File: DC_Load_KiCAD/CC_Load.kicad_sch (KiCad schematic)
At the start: 64 parts, among them J1 VoltSense_Conn, J2 PowerInput_Conn, J3 LED_Conn, J4 Load_Conn, J5 16x2_LCD_Conn, J6 RotEnc_Conn, J7 Fan_Conn, Q1 IRLZ44N, Q2 IRLZ44N, Q3 IRLZ44N, Q4 IRLZ44N, Q5 IRLZ44N, U1 LM7805_TO220, U2 LM358

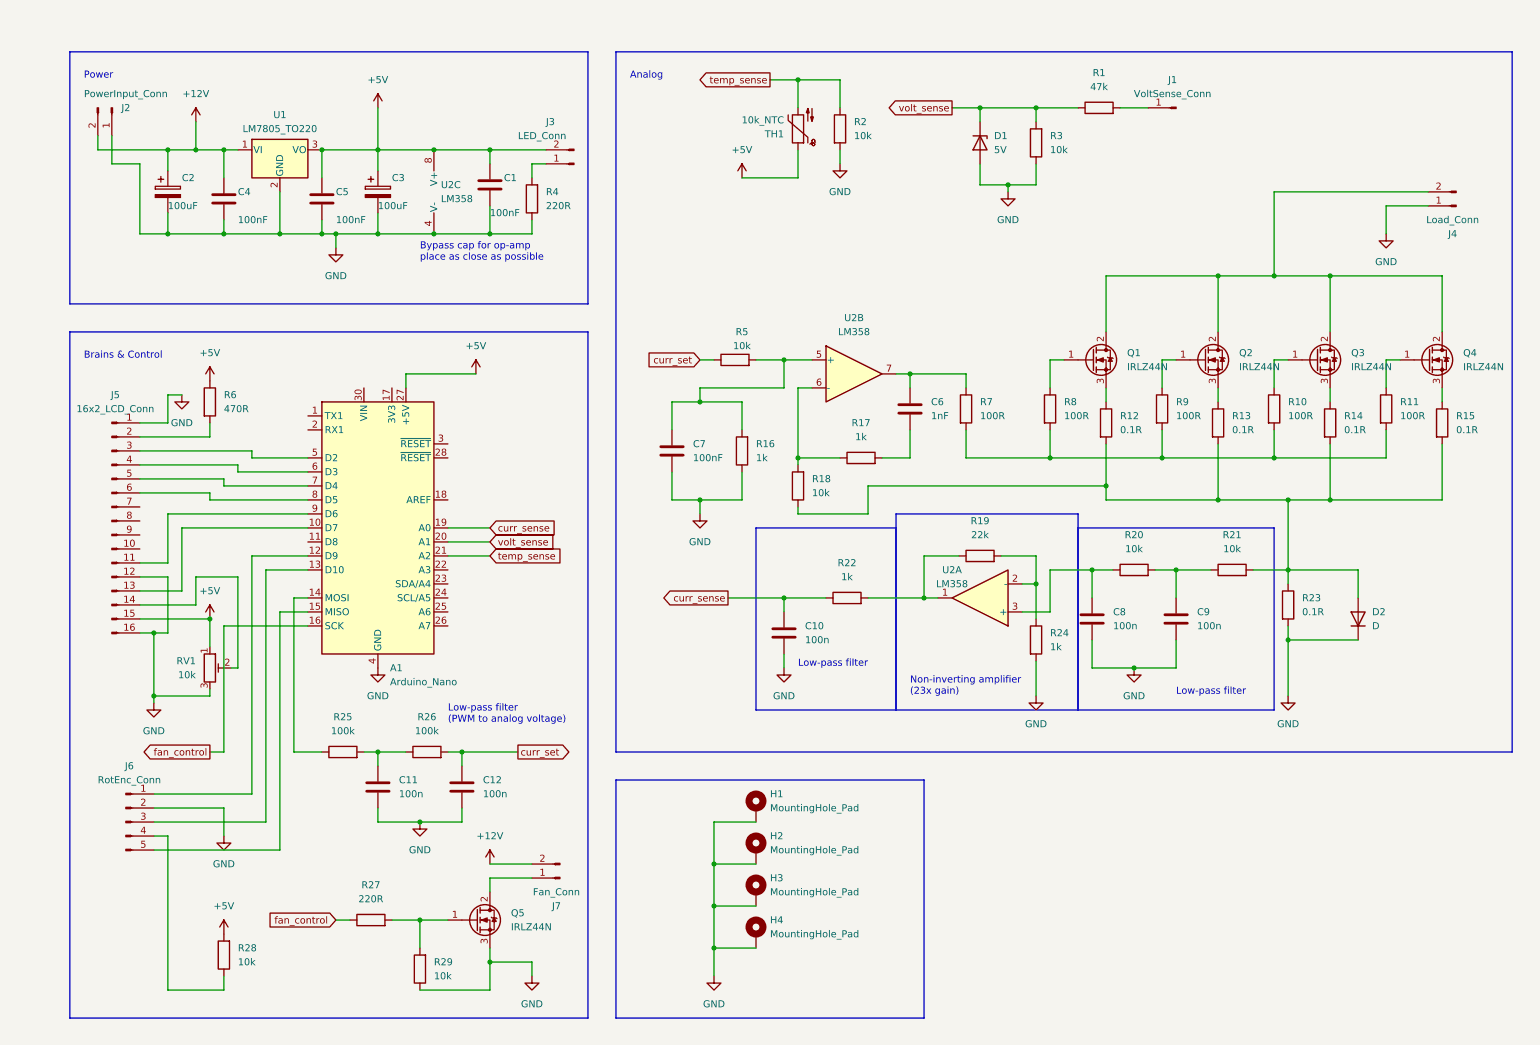
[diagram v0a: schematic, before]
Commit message: Update PCB and prepare for ordering
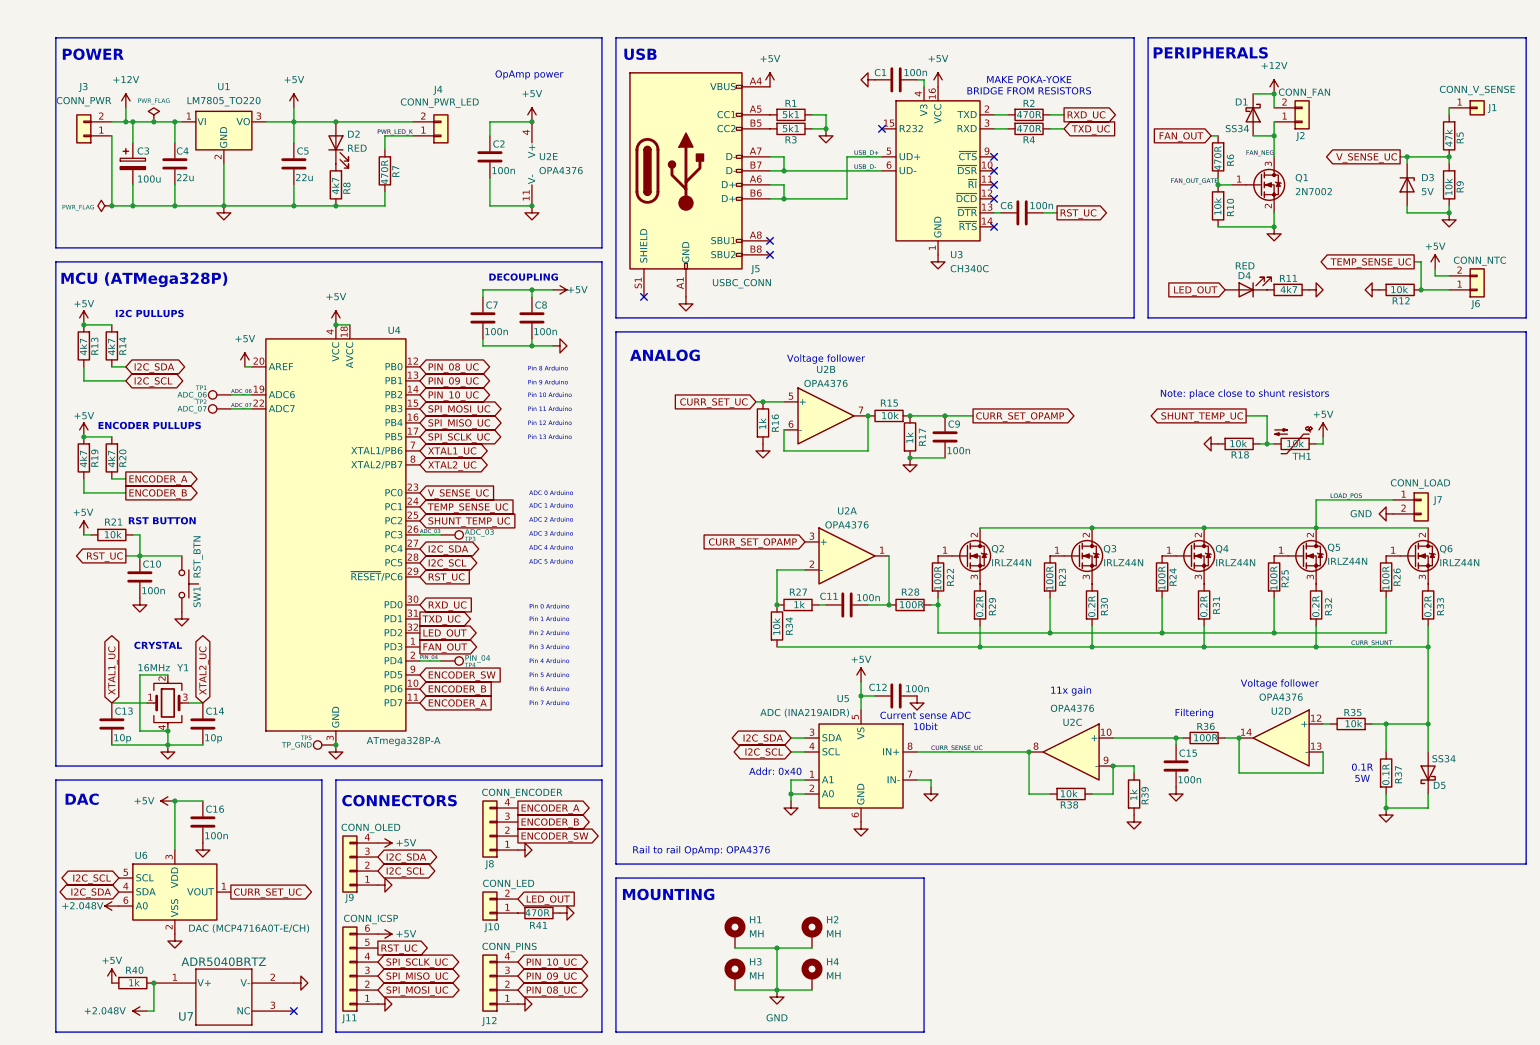
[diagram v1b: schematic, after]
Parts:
- removed A1: Arduino_Nano, Module:Arduino_Nano, symbol MCU_Module:Arduino_Nano_Every
- removed C2: 100uF, Capacitor_THT:CP_Radial_D6.3mm_P2.50mm, symbol Device:C_Polarized
- removed D1: 5V, Diode_THT:D_T-1_P5.08mm_Horizontal, symbol Device:D_Zener
- removed D2: D, Diode_THT:D_T-1_P5.08mm_Horizontal, symbol Device:D
- removed J1: VoltSense_Conn, MyFootprintLibrary:ScrewTerminal_01x02_P5mm, symbol Connector:Conn_01x01_Pin
- removed J2: PowerInput_Conn, MyFootprintLibrary:ScrewTerminal_01x02_P5mm, symbol Connector:Conn_01x02_Pin
- removed J3: LED_Conn, Connector_PinHeader_2.54mm:PinHeader_1x02_P2.54mm_Vertical, symbol Connector:Conn_01x02_Pin
- removed J4: Load_Conn, MyFootprintLibrary:ScrewTerminal_01x02_P5mm, symbol Connector:Conn_01x02_Pin
- removed J5: 16x2_LCD_Conn, Connector_PinHeader_2.54mm:PinHeader_1x16_P2.54mm_Vertical, symbol Connector:Conn_01x16_Pin
- removed J6: RotEnc_Conn, Connector_PinHeader_2.54mm:PinHeader_1x05_P2.54mm_Vertical, symbol Connector:Conn_01x05_Pin
- removed J7: Fan_Conn, Connector_PinHeader_2.54mm:PinHeader_1x02_P2.54mm_Vertical, symbol Connector:Conn_01x02_Pin
- removed Q5: IRLZ44N, Package_TO_SOT_THT:TO-220-3_Vertical, symbol Transistor_FET:IRLZ44N
- removed R23: 0.1R, Resistor_THT:R_Axial_Power_L25.0mm_W9.0mm_P27.94mm, symbol Device:R
- removed R24: 1k, Resistor_SMD:R_1206_3216Metric, symbol Device:R
- removed R25, R26: 100k, Resistor_SMD:R_1206_3216Metric, symbol Device:R
- removed R7: 100R, Resistor_SMD:R_1206_3216Metric, symbol Device:R
- removed RV1: 10k, Connector_PinHeader_2.54mm:PinHeader_1x03_P2.54mm_Vertical, symbol Device:R_Potentiometer_Trim
- removed U2: LM358, Package_DIP:DIP-8_W7.62mm_LongPads, symbol Amplifier_Operational:LM358
- added C13, C14: 10p, Capacitor_SMD:C_0805_2012Metric, symbol Device:C
- added C15, C16, C2: 100n, Capacitor_SMD:C_1206_3216Metric, symbol Device:C
- added D1, D5: SS34, Diode_SMD:D_SMA, symbol Diode:SS34
- added D2, D4: RED, LED_SMD:LED_1210_3225Metric, symbol Device:LED
- added D3: 5V, Diode_SMD:D_SOD-123, symbol Device:D_Zener
- added J1: CONN_V_SENSE, Connector_PinHeader_2.54mm:PinHeader_1x01_P2.54mm_Vertical, symbol Connector_Generic:Conn_01x01
- added J10: CONN_LED, Connector_PinHeader_2.54mm:PinHeader_1x02_P2.54mm_Vertical, symbol Connector_Generic:Conn_01x02
- added J11: CONN_ICSP, Connector_PinHeader_2.54mm:PinHeader_1x06_P2.54mm_Vertical, symbol Connector_Generic:Conn_01x06
- added J12: CONN_PINS, Connector_PinHeader_2.54mm:PinHeader_1x04_P2.54mm_Vertical, symbol Connector_Generic:Conn_01x04
- added J2: CONN_FAN, Connector_PinHeader_2.54mm:PinHeader_1x02_P2.54mm_Vertical, symbol Connector_Generic:Conn_01x02
- added J3: CONN_PWR, Connector_PinHeader_2.54mm:PinHeader_1x02_P2.54mm_Vertical, symbol Connector_Generic:Conn_01x02
- added J4: CONN_PWR_LED, Connector_PinHeader_2.54mm:PinHeader_1x02_P2.54mm_Vertical, symbol Connector_Generic:Conn_01x02
- added J5: USBC_CONN, Connector_USB:USB_C_Receptacle_G-Switch_GT-USB-7010ASV, symbol Connector:USB_C_Receptacle_USB2.0
- added J6: CONN_NTC, Connector_PinHeader_2.54mm:PinHeader_1x02_P2.54mm_Vertical, symbol Connector_Generic:Conn_01x02
- added J7: CONN_LOAD, Connector_PinHeader_2.54mm:PinHeader_1x02_P2.54mm_Vertical, symbol Connector_Generic:Conn_01x02
- added J8: CONN_ENCODER, Connector_PinHeader_2.54mm:PinHeader_1x04_P2.54mm_Vertical, symbol Connector_Generic:Conn_01x04
- added J9: CONN_OLED, Connector_PinHeader_2.54mm:PinHeader_1x04_P2.54mm_Vertical, symbol Connector_Generic:Conn_01x04
- added Q1: 2N7002, Package_TO_SOT_SMD:SOT-23, symbol Transistor_FET:2N7002
- added Q2: IRLZ44N, Package_TO_SOT_THT:TO-220-3_Vertical, symbol Transistor_FET:IRLZ44N
- added R10, R12, R15, R34, R35, R38, R9: 10k, Resistor_SMD:R_1206_3216Metric, symbol Device:R
- added R11, R13, R14, R8: 4k7, Resistor_SMD:R_1206_3216Metric, symbol Device:R
- added R36: 100R, Resistor_SMD:R_1206_3216Metric, symbol Device:R
- added R37: 0.1R, Resistor_THT:R_Axial_Power_L25.0mm_W9.0mm_P27.94mm, symbol Device:R
- added R39, R40: 1k, Resistor_SMD:R_1206_3216Metric, symbol Device:R
- added R4, R41: 470R, Resistor_SMD:R_1206_3216Metric, symbol Device:R
- added SW1: RST_BTN, Button_Switch_THT:SW_PUSH_6mm, symbol Switch:SW_Push
- added TP1: ADC_06, TestPoint:TestPoint_THTPad_1.5x1.5mm_Drill0.7mm, symbol Connector:TestPoint
- added TP2: ADC_07, TestPoint:TestPoint_THTPad_1.5x1.5mm_Drill0.7mm, symbol Connector:TestPoint
- added TP3: ADC_03, TestPoint:TestPoint_THTPad_1.5x1.5mm_Drill0.7mm, symbol Connector:TestPoint
- added TP4: PIN_04, TestPoint:TestPoint_THTPad_1.5x1.5mm_Drill0.7mm, symbol Connector:TestPoint
- added TP5: TP_GND, TestPoint:TestPoint_THTPad_1.5x1.5mm_Drill0.7mm, symbol Connector:TestPoint
- added U2: OPA4376, Package_SO:TSSOP-14_4.4x5mm_P0.65mm, symbol Amplifier_Operational:OPA4376
- added U3: CH340C, Package_SO:SOIC-16_3.9x9.9mm_P1.27mm, symbol Interface_USB:CH340C
- added U4: ATmega328P-A, Package_QFP:TQFP-32_7x7mm_P0.8mm, symbol MCU_Microchip_ATmega:ATmega328P-A
- added U5: ADC (INA219AIDR), Package_SO:SOIC-8_3.9x4.9mm_P1.27mm, symbol Sensor_Energy:INA219AxD
- added U6: DAC (MCP4716A0T-E/CH), Package_TO_SOT_SMD:SOT-23-6, symbol Analog_DAC:MCP4725xxx-xCH
- added U7: ADR5040BRTZ, Package_TO_SOT_SMD:SOT-23, symbol 2024-04-29_11-10-47:ADR5040BRTZ-REEL7
- added Y1: 16MHz, Crystal:Crystal_SMD_3225-4Pin_3.2x2.5mm, symbol Device:Crystal_GND24
- C1, C7: value 100nF -> 100n
- C3: value 100uF -> 100u; footprint Capacitor_THT:CP_Radial_D6.3mm_P2.50mm -> Capacitor_SMD:CP_Elec_8x10.5
- C4, C5: value 100nF -> 22u; footprint Capacitor_SMD:C_1206_3216Metric -> Capacitor_SMD:C_0805_2012Metric
- C6: value 1nF -> 100n
- H1, H4: value MountingHole_Pad -> MH
- H2: renamed from H3; value MountingHole_Pad -> MH
- H3: renamed from H2; value MountingHole_Pad -> MH
- R1: value 47k -> 5k1; footprint Resistor_SMD:R_1206_3216Metric -> Resistor_SMD:R_0805_2012Metric
- R19: value 22k -> 4k7
- R2: value 10k -> 470R
- R20: value 10k -> 4k7
- R22: value 1k -> 100R
- R27: value 220R -> 1k
- R28: value 10k -> 100R
- R29: value 10k -> 0.2R
- R3: value 10k -> 5k1; footprint Resistor_SMD:R_1206_3216Metric -> Resistor_SMD:R_0805_2012Metric
- R30: renamed from R12; value 0.1R -> 0.2R; footprint Resistor_THT:R_Axial_Power_L25.0mm_W9.0mm_P27.94mm -> Resistor_SMD:R_1206_3216Metric
- R31: renamed from R13; value 0.1R -> 0.2R; footprint Resistor_THT:R_Axial_Power_L25.0mm_W9.0mm_P27.94mm -> Resistor_SMD:R_1206_3216Metric
- R32: renamed from R14; value 0.1R -> 0.2R; footprint Resistor_THT:R_Axial_Power_L25.0mm_W9.0mm_P27.94mm -> Resistor_SMD:R_1206_3216Metric
- R33: renamed from R15; value 0.1R -> 0.2R; footprint Resistor_THT:R_Axial_Power_L25.0mm_W9.0mm_P27.94mm -> Resistor_SMD:R_1206_3216Metric
- R5: value 10k -> 47k
- R7: renamed from R4; value 220R -> 470R
- TH1: value 10k_NTC -> 10k; footprint Connector_PinHeader_2.54mm:PinHeader_1x02_P2.54mm_Vertical -> Resistor_SMD:R_0805_2012Metric
- renumbered Q1 to Q3, Q2 to Q4, Q3 to Q5, Q4 to Q6, R8 to R23, R9 to R24, R10 to R25, R11 to R26
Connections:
- net +12V: now also C3.1, D1.1 (K), J2.2 (Pin_2), J3.2 (Pin_2)
- net +5V: now also C12.1, C7.1, C8.1, R19.2, R20.2, R21.2, C16.1, C2.1, D2.2 (A), J11.6 (Pin_6), J4.2 (Pin_2), J5.A4 (VBUS), J5.A9 (VBUS), J5.B4 (VBUS), J5.B9 (VBUS), J6.2 (Pin_2), J9.4 (Pin_4), R13.2, R14.2, R40.2, U2.4 (V+), U3.16 (VCC), U4.18 (AVCC), U4.20 (AREF), U4.4 (VCC), U4.6 (VCC), U5.5 (VS), U6.3 (VDD); no longer C1.1, C3.1, R28.2, R6.1
- net GND: now also C1.1, R1.1, R16.2, R17.2, R18.2, C13.2, C14.2, C15.2, C16.2, C2.2, D3.2 (A), D5.1 (K), J11.1 (Pin_1), J12.1 (Pin_1), J3.1 (Pin_1), J5.A1 (GND), J5.A12 (GND), J5.B1 (GND), J5.B12 (GND), J7.2 (Pin_2), J8.1 (Pin_1), J9.1 (Pin_1), Q1.2 (S), R10.1, R11.1, R12.2, R37.2, R39.2, R41.1, R8.1, R9.1, SW1.2, TP5.1, U2.11 (V-), U3.1 (GND), U4.21 (GND), U4.3 (GND), U4.5 (GND), U5.1 (A1), U5.2 (A0), U5.6 (GND), U5.7 (IN-), U6.2 (VSS), U7.2 (V-), Y1.2, Y1.4; no longer C1.2, C11.2, R16.1, R2.2, R29.1
- net CURR_SHUNT: now reaches R30.2, R31.2, R32.2, R33.2
- net CURR_SHUNT: now also R29.2, D5.2 (A), R34.2, R35.2, R37.1; no longer R18.1, R21.2
- net at R22.2: now also R23.2, R24.2, R25.2, R26.2, R28.2; no longer R19.1
- net ENCODER_A: now reaches R20.1
- net ENCODER_A: now also J8.4 (Pin_4), U4.11 (PD7); no longer C8.1
- net PWR_LED_K: now reaches R7.2
- net PWR_LED_K: now also J4.1 (Pin_1)
- net FAN_OUT: now reaches R6.2
- net FAN_OUT: now also U4.1 (PD3)
- net at R28.1: now also C11.2, U2.1
- net at C6.1: now also U3.13 (~{DTR})
- net at R27.2: now also C11.1; no longer R29.2
- net LOAD_POS: now reaches Q3.2 (D), Q4.2 (D), Q5.2 (D), Q6.2 (D)
- net LOAD_POS: now also J7.1 (Pin_1), Q2.2 (D)
- net at R1.2: now also J5.A5 (CC1)
- net RST_UC: now reaches C6.2
- net RST_UC: now also C10.1, R21.1, J11.5 (Pin_5), SW1.1, U4.29 (~{RESET}/PC6); no longer R17.2
- net CURR_SET_OPAMP: now reaches R17.1
- net CURR_SET_OPAMP: now also C9.1, R15.2, U2.3 (+); no longer R18.2
- net curr_sense: no longer names the net of R22.1
- net curr_sense: now also Q2.1 (G); no longer C10.1
- net curr_set renamed V_SENSE_UC
- net V_SENSE_UC: now also D3.1 (K), R9.2, U4.23 (PC0); no longer C12.1
- net fan_control: no longer names the net of R27.1
- net fan_control: now also R34.1, U2.2 (-)
- net temp_sense renamed RXD_UC
- net RXD_UC: now also U4.30 (PD0); no longer TH1.2
- net volt_sense: no longer names the net of R3.2
- net volt_sense: now also J5.B5 (CC2); no longer R1.1
- new net: C1.2, U3.4 (V3)
- new net: J1.1 (Pin_1), R5.2
- new net: R35.1, U2.12 (+)
- new net: R38.1, R39.1, U2.9 (-)
- new net: J10.1 (Pin_1), R41.2
- new net: Q2.3 (S), R29.1
- new net: R36.2, U2.13 (-), U2.14
- new net: C15.1, R36.1, U2.10 (+)
- new net: D2.1 (K), R8.2
- new net: R15.1, U2.6 (-), U2.7
- new net: D4.1 (K), R11.2
- new net: R2.2, U3.2 (TXD)
- new net: R4.2, U3.3 (RXD)
- new net +2.048V: R40.1, U6.6 (A0), U7.1 (V+)
- new net ADC_03: TP3.1, U4.26 (PC3)
- new net ADC_06: TP1.1, U4.19 (ADC6)
- new net ADC_07: TP2.1, U4.22 (ADC7)
- new net CURR_SENSE_UC: R38.2, U2.8, U5.8 (IN+)
- new net CURR_SET_UC: R16.1, U2.5 (+), U6.1 (VOUT)
- new net ENCODER_B: J8.3 (Pin_3), R19.1, U4.10 (PD6)
- new net ENCODER_SW: J8.2 (Pin_2), U4.9 (PD5)
- new net FAN_NEG: D1.2 (A), J2.1 (Pin_1), Q1.3 (D)
- new net FAN_OUT_GATE: Q1.1 (G), R10.2, R6.1
- new net I2C_SCL: J9.2 (Pin_2), R13.1, U4.28 (PC5), U5.4 (SCL), U6.5 (SCL)
- new net I2C_SDA: J9.3 (Pin_3), R14.1, U4.27 (PC4), U5.3 (SDA), U6.4 (SDA)
- new net LED_OUT: D4.2 (A), J10.2 (Pin_2), U4.32 (PD2)
- new net PIN_04: TP4.1, U4.2 (PD4)
- new net PIN_08_UC: J12.2 (Pin_2), U4.12 (PB0)
- new net PIN_09_UC: J12.3 (Pin_3), U4.13 (PB1)
- new net PIN_10_UC: J12.4 (Pin_4), U4.14 (PB2)
- new net SHUNT_TEMP_UC: R18.1, TH1.2, U4.25 (PC2)
- new net SPI_MISO_UC: J11.3 (Pin_3), U4.16 (PB4)
- new net SPI_MOSI_UC: J11.2 (Pin_2), U4.15 (PB3)
- new net SPI_SCLK_UC: J11.4 (Pin_4), U4.17 (PB5)
- new net TEMP_SENSE_UC: J6.1 (Pin_1), R12.1, U4.24 (PC1)
- new net TXD_UC: R4.1, U4.31 (PD1)
- new net USB_D+: J5.A6 (D+), J5.B6 (D+), U3.5 (UD+)
- new net USB_D-: J5.A7 (D-), J5.B7 (D-), U3.6 (UD-)
- new net XTAL1_UC: C13.1, U4.7 (XTAL1/PB6), Y1.1
- new net XTAL2_UC: C14.1, U4.8 (XTAL2/PB7), Y1.3
- no-connect marks 0 -> 10
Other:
- note added: "0.1R 5W"
- note added: "11x gain"
- note added: "ADC 0 Arduino"
- note added: "ADC 1 Arduino"
- note added: "ADC 2 Arduino"
- note added: "ADC 3 Arduino"
- note added: "ADC 4 Arduino"
- note added: "ADC 5 Arduino"
- note added: "ANALOG"
- note added: "Addr: 0x40"
- note added: "CONNECTORS"
- note added: "CRYSTAL"
- note added: "Current sense ADC 10bit"
- note added: "DAC"
- note added: "DECOUPLING"
- note added: "ENCODER PULLUPS"
- note added: "Filtering"
- note added: "I2C PULLUPS"
- note added: "MAKE POKA-YOKE BRIDGE FROM RESISTORS"
- note added: "MCU (ATMega328P)"
- note added: "MOUNTING"
- note added: "Note: place close to shunt resistors"
- note added: "OpAmp power"
- note added: "PERIPHERALS"
- note added: "POWER"
- note added: "Pin 0 Arduino"
- note added: "Pin 1 Arduino"
- note added: "Pin 10 Arduino"
- note added: "Pin 11 Arduino"
- note added: "Pin 12 Arduino"
- note added: "Pin 13 Arduino"
- note added: "Pin 2 Arduino"
- note added: "Pin 3 Arduino"
- note added: "Pin 4 Arduino"
- note added: "Pin 5 Arduino"
- note added: "Pin 6 Arduino"
- note added: "Pin 7 Arduino"
- note added: "Pin 8 Arduino"
- note added: "Pin 9 Arduino"
- note added: "RST BUTTON"
- note added: "Rail to rail OpAmp: OPA4376"
- note added: "USB"
- note added: "Voltage follower"
- note removed: "Analog"
- note removed: "Brains & Control"
- note removed: "Bypass cap for op-amp place as close as possible"
- note removed: "Low-pass filter"
- note removed: "Low-pass filter (PWM to analog voltage)"
- note removed: "Non-inverting amplifier (23x gain)"
- note removed: "Power"
- company: (none) -> Aleksa Heler
- title: (none) -> DC Programmable Load
- moved on the sheet: C5, H1, H2, H3, H4, Q3, Q4, Q5, Q6, R23, R24, R25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

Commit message: Added comments for future improvements, successfully flashed one device
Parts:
- C13, C14: value 10p -> 20p
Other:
- note added: "RST still doesnt work properly, not with CH340 and neither with FTDI board"
- note added: "TODO: Add footprint for jumper capacitor 100n for RST here!"
- note added: "TODO: Put RX/TX signals on some pin header for easy reprogramming"
- note added: "this RST cap might not be needed!"
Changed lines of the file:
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@@
 		)
 	)
+	(text "RST still doesnt work properly,\nnot with CH340 and neither with\nFTDI board"
+		(exclude_from_sim no)
+		(at 186.69 55.88 0)
+		(effects
+			(font
+				(size 2 2)
+				(thickness 0.4)
+				(bold yes)
+			)
+			(justify left)
+		)
+	)
 	(text "I2C PULLUPS"
 		(exclude_from_sim no)
@@
 		)
 	)
+	(text "this RST cap \nmight not be needed!"
+		(exclude_from_sim no)
+		(at 7.112 115.062 0)
+		(effects
+			(font
+				(size 2 2)
+				(thickness 0.4)
+				(bold yes)
+			)
+			(justify left)
+		)
+	)
 	(text "CONNECTORS"
 		(exclude_from_sim no)
@@
 		)
 	)
+	(text "TODO:\nPut RX/TX signals\non some pin header\nfor easy reprogramming"
+		(exclude_from_sim no)
+		(at 175.006 17.526 0)
+		(effects
+			(font
+				(size 2 2)
+				(thickness 0.4)
+				(bold yes)
+			)
+			(justify left)
+		)
+	)
 	(text "Pin 11 Arduino"
 		(exclude_from_sim no)
@@
 		)
 	)
+	(text "TODO:\nAdd footprint for jumper \ncapacitor 100n for RST here!"
+		(exclude_from_sim no)
+		(at 66.548 190.754 0)
+		(effects
+			(font
+				(size 2 2)
+				(thickness 0.4)
+				(bold yes)
+			)
+			(justify left)
+		)
+	)
 	(text "Pin 6 Arduino"
 		(exclude_from_sim no)
@@
 			)
 		)
-		(property "Value" "10p"
+		(property "Value" "20p"
 			(at 25.654 142.24 0)
 			(effects
@@
 			)
 		)
-		(property "Value" "10p"
+		(property "Value" "20p"
 			(at 42.164 142.24 0)
 			(effects

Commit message: Update initial code with simple drivers
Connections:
- net SHUNT_TEMP_UC renamed PCB_TEMP_UC
